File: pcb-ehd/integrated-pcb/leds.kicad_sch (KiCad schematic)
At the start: 41 parts, among them U6 SN74LVC1T45DCK

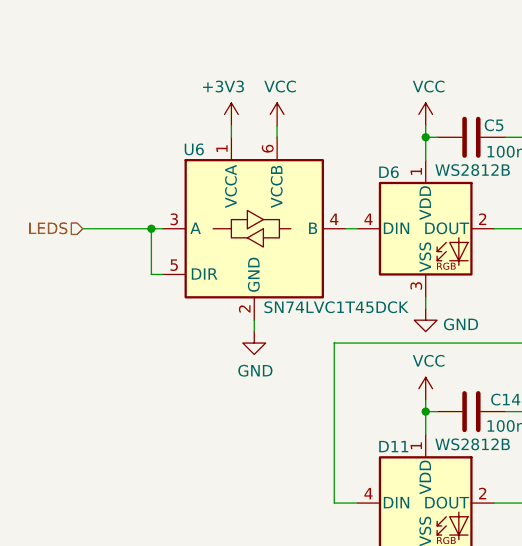
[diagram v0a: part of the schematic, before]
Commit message: rough placement of all but analog
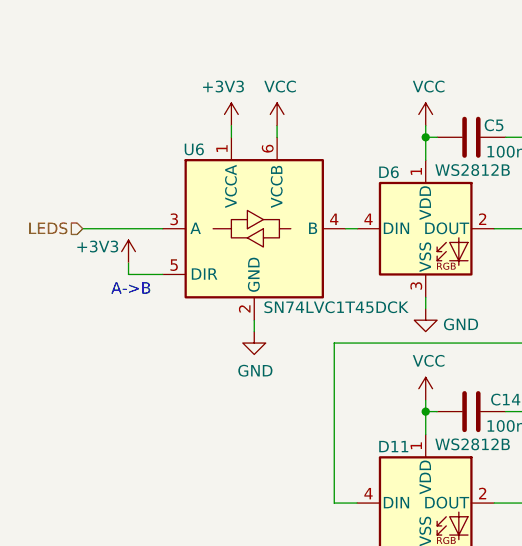
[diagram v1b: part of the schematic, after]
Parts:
- D10, D11, D12, D13, D14, D15, D16, D17, D18, D19, D20, D21, D22, D23, D24, D25, D6, D7, D8, D9: footprint LED_SMD:LED_WS2812B_PLCC4_5.0x5.0mm_P3.2mm -> ehd:LED_WS2812B_PLCC4_5.0x5.0mm_P3.2mm
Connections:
- net +3V3: now also U6.5 (DIR)
- net LEDS: no longer U6.5 (DIR)
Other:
- note added: "A->B"
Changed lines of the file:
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@@
     (company "Josh Johnson")
   )
-  (junction (at 77.47 53.34) (diameter 0.9144) (color 0 0 0 0))
   (junction (at 107.95 43.18) (diameter 0.9144) (color 0 0 0 0))
   (junction (at 107.95 73.66) (diameter 0.9144) (color 0 0 0 0))
@@
   (junction (at 189.23 134.62) (diameter 0.9144) (color 0 0 0 0))
   (no_connect (at 196.85 144.78))
-  (wire (pts (xy 69.85 53.34) (xy 77.47 53.34))
-    (stroke (width 0) (type solid) (color 0 0 0 0))
-  )
-  (wire (pts (xy 77.47 53.34) (xy 77.47 58.42))
-    (stroke (width 0) (type solid) (color 0 0 0 0))
-  )
-  (wire (pts (xy 77.47 53.34) (xy 78.74 53.34))
-    (stroke (width 0) (type solid) (color 0 0 0 0))
-  )
-  (wire (pts (xy 78.74 58.42) (xy 77.47 58.42))
+  (wire (pts (xy 69.85 53.34) (xy 78.74 53.34))
+    (stroke (width 0) (type solid) (color 0 0 0 0))
+  )
+  (wire (pts (xy 74.93 58.42) (xy 74.93 57.15))
+    (stroke (width 0) (type solid) (color 0 0 0 0))
+  )
+  (wire (pts (xy 74.93 58.42) (xy 78.74 58.42))
     (stroke (width 0) (type solid) (color 0 0 0 0))
   )
@@
   (wire (pts (xy 201.93 135.89) (xy 201.93 134.62))
     (stroke (width 0) (type solid) (color 0 0 0 0))
+  )
+  (text "A->B" (at 77.47 60.96 180)
+    (effects (font (size 1.27 1.27)) (justify right bottom))
   )
   (text "Bow Tie LEDs" (at 157.48 34.29 180)
@@
   (hierarchical_label "LEDS" (shape input) (at 69.85 53.34 180)
     (effects (font (size 1.27 1.27)) (justify right))
+  )
+  (symbol (lib_id "power:+3V3") (at 74.93 57.15 0) (unit 1)
+    (in_bom yes) (on_board yes)
+    (property "Reference" "#PWR0197" (id 0) (at 74.93 60.96 0)
+      (effects (font (size 1.27 1.27)) hide)
+    )
+    (property "Value" "+3V3" (id 1) (at 71.4883 55.3656 0))
+    (property "Footprint" "" (id 2) (at 74.93 57.15 0)
+      (effects (font (size 1.27 1.27)) hide)
+    )
+    (property "Datasheet" "" (id 3) (at 74.93 57.15 0)
+      (effects (font (size 1.27 1.27)) hide)
+    )
+    (pin "1")
   )
   (symbol (lib_id "power:+3V3") (at 86.36 41.91 0) (unit 1)
@@
       (effects (font (size 1.27 1.27)) (justify left))
     )
-    (property "Footprint" "LED_SMD:LED_WS2812B_PLCC4_5.0x5.0mm_P3.2mm" (id 2) (at 109.22 60.96 0)
+    (property "Footprint" "ehd:LED_WS2812B_PLCC4_5.0x5.0mm_P3.2mm" (id 2) (at 109.22 60.96 0)
       (effects (font (size 1.27 1.27)) (justify left top) hide)
     )
@@
       (effects (font (size 1.27 1.27)) (justify left))
     )
-    (property "Footprint" "LED_SMD:LED_WS2812B_PLCC4_5.0x5.0mm_P3.2mm" (id 2) (at 109.22 91.44 0)
+    (property "Footprint" "ehd:LED_WS2812B_PLCC4_5.0x5.0mm_P3.2mm" (id 2) (at 109.22 91.44 0)
       (effects (font (size 1.27 1.27)) (justify left top) hide)
     )
@@
       (effects (font (size 1.27 1.27)) (justify left))
     )
-    (property "Footprint" "LED_SMD:LED_WS2812B_PLCC4_5.0x5.0mm_P3.2mm" (id 2) (at 109.22 121.92 0)
+    (property "Footprint" "ehd:LED_WS2812B_PLCC4_5.0x5.0mm_P3.2mm" (id 2) (at 109.22 121.92 0)
       (effects (font (size 1.27 1.27)) (justify left top) hide)
     )
@@
       (effects (font (size 1.27 1.27)) (justify left))
     )
-    (property "Footprint" "LED_SMD:LED_WS2812B_PLCC4_5.0x5.0mm_P3.2mm" (id 2) (at 109.22 152.4 0)
+    (property "Footprint" "ehd:LED_WS2812B_PLCC4_5.0x5.0mm_P3.2mm" (id 2) (at 109.22 152.4 0)
       (effects (font (size 1.27 1.27)) (justify left top) hide)
     )
@@
       (effects (font (size 1.27 1.27)) (justify left))
     )
-    (property "Footprint" "LED_SMD:LED_WS2812B_PLCC4_5.0x5.0mm_P3.2mm" (id 2) (at 129.54 60.96 0)
+    (property "Footprint" "ehd:LED_WS2812B_PLCC4_5.0x5.0mm_P3.2mm" (id 2) (at 129.54 60.96 0)
       (effects (font (size 1.27 1.27)) (justify left top) hide)
     )
@@
       (effects (font (size 1.27 1.27)) (justify left))
     )
-    (property "Footprint" "LED_SMD:LED_WS2812B_PLCC4_5.0x5.0mm_P3.2mm" (id 2) (at 129.54 91.44 0)
+    (property "Footprint" "ehd:LED_WS2812B_PLCC4_5.0x5.0mm_P3.2mm" (id 2) (at 129.54 91.44 0)
       (effects (font (size 1.27 1.27)) (justify left top) hide)
     )
@@
       (effects (font (size 1.27 1.27)) (justify left))
     )
-    (property "Footprint" "LED_SMD:LED_WS2812B_PLCC4_5.0x5.0mm_P3.2mm" (id 2) (at 129.54 121.92 0)
+    (property "Footprint" "ehd:LED_WS2812B_PLCC4_5.0x5.0mm_P3.2mm" (id 2) (at 129.54 121.92 0)
       (effects (font (size 1.27 1.27)) (justify left top) hide)
     )
@@
       (effects (font (size 1.27 1.27)) (justify left))
     )
-    (property "Footprint" "LED_SMD:LED_WS2812B_PLCC4_5.0x5.0mm_P3.2mm" (id 2) (at 129.54 152.4 0)
+    (property "Footprint" "ehd:LED_WS2812B_PLCC4_5.0x5.0mm_P3.2mm" (id 2) (at 129.54 152.4 0)
       (effects (font (size 1.27 1.27)) (justify left top) hide)
     )
@@
       (effects (font (size 1.27 1.27)) (justify left))
     )
-    (property "Footprint" "LED_SMD:LED_WS2812B_PLCC4_5.0x5.0mm_P3.2mm" (id 2) (at 149.86 60.96 0)
+    (property "Footprint" "ehd:LED_WS2812B_PLCC4_5.0x5.0mm_P3.2mm" (id 2) (at 149.86 60.96 0)
       (effects (font (size 1.27 1.27)) (justify left top) hide)
     )
@@
       (effects (font (size 1.27 1.27)) (justify left))
     )
-    (property "Footprint" "LED_SMD:LED_WS2812B_PLCC4_5.0x5.0mm_P3.2mm" (id 2) (at 149.86 91.44 0)
+    (property "Footprint" "ehd:LED_WS2812B_PLCC4_5.0x5.0mm_P3.2mm" (id 2) (at 149.86 91.44 0)
       (effects (font (size 1.27 1.27)) (justify left top) hide)
     )
@@
       (effects (font (size 1.27 1.27)) (justify left))
     )
-    (property "Footprint" "LED_SMD:LED_WS2812B_PLCC4_5.0x5.0mm_P3.2mm" (id 2) (at 149.86 121.92 0)
+    (property "Footprint" "ehd:LED_WS2812B_PLCC4_5.0x5.0mm_P3.2mm" (id 2) (at 149.86 121.92 0)
       (effects (font (size 1.27 1.27)) (justify left top) hide)
     )
@@
       (effects (font (size 1.27 1.27)) (justify left))
     )
-    (property "Footprint" "LED_SMD:LED_WS2812B_PLCC4_5.0x5.0mm_P3.2mm" (id 2) (at 149.86 152.4 0)
+    (property "Footprint" "ehd:LED_WS2812B_PLCC4_5.0x5.0mm_P3.2mm" (id 2) (at 149.86 152.4 0)
       (effects (font (size 1.27 1.27)) (justify left top) hide)
     )
@@
       (effects (font (size 1.27 1.27)) (justify left))
     )
-    (property "Footprint" "LED_SMD:LED_WS2812B_PLCC4_5.0x5.0mm_P3.2mm" (id 2) (at 170.18 60.96 0)
+    (property "Footprint" "ehd:LED_WS2812B_PLCC4_5.0x5.0mm_P3.2mm" (id 2) (at 170.18 60.96 0)
       (effects (font (size 1.27 1.27)) (justify left top) hide)
     )
@@
       (effects (font (size 1.27 1.27)) (justify left))
     )
-    (property "Footprint" "LED_SMD:LED_WS2812B_PLCC4_5.0x5.0mm_P3.2mm" (id 2) (at 170.18 91.44 0)
+    (property "Footprint" "ehd:LED_WS2812B_PLCC4_5.0x5.0mm_P3.2mm" (id 2) (at 170.18 91.44 0)
       (effects (font (size 1.27 1.27)) (justify left top) hide)
     )
@@
       (effects (font (size 1.27 1.27)) (justify left))
     )
-    (property "Footprint" "LED_SMD:LED_WS2812B_PLCC4_5.0x5.0mm_P3.2mm" (id 2) (at 170.18 121.92 0)
+    (property "Footprint" "ehd:LED_WS2812B_PLCC4_5.0x5.0mm_P3.2mm" (id 2) (at 170.18 121.92 0)
       (effects (font (size 1.27 1.27)) (justify left top) hide)
     )
@@
       (effects (font (size 1.27 1.27)) (justify left))
     )
-    (property "Footprint" "LED_SMD:LED_WS2812B_PLCC4_5.0x5.0mm_P3.2mm" (id 2) (at 170.18 152.4 0)
+    (property "Footprint" "ehd:LED_WS2812B_PLCC4_5.0x5.0mm_P3.2mm" (id 2) (at 170.18 152.4 0)
       (effects (font (size 1.27 1.27)) (justify left top) hide)
     )
@@
       (effects (font (size 1.27 1.27)) (justify left))
     )
-    (property "Footprint" "LED_SMD:LED_WS2812B_PLCC4_5.0x5.0mm_P3.2mm" (id 2) (at 190.5 60.96 0)
+    (property "Footprint" "ehd:LED_WS2812B_PLCC4_5.0x5.0mm_P3.2mm" (id 2) (at 190.5 60.96 0)
       (effects (font (size 1.27 1.27)) (justify left top) hide)
     )
@@
       (effects (font (size 1.27 1.27)) (justify left))
     )
-    (property "Footprint" "LED_SMD:LED_WS2812B_PLCC4_5.0x5.0mm_P3.2mm" (id 2) (at 190.5 91.44 0)
+    (property "Footprint" "ehd:LED_WS2812B_PLCC4_5.0x5.0mm_P3.2mm" (id 2) (at 190.5 91.44 0)
       (effects (font (size 1.27 1.27)) (justify left top) hide)
     )
@@
       (effects (font (size 1.27 1.27)) (justify left))
     )
-    (property "Footprint" "LED_SMD:LED_WS2812B_PLCC4_5.0x5.0mm_P3.2mm" (id 2) (at 190.5 121.92 0)
+    (property "Footprint" "ehd:LED_WS2812B_PLCC4_5.0x5.0mm_P3.2mm" (id 2) (at 190.5 121.92 0)
       (effects (font (size 1.27 1.27)) (justify left top) hide)
     )
@@
       (effects (font (size 1.27 1.27)) (justify left))
     )
-    (property "Footprint" "LED_SMD:LED_WS2812B_PLCC4_5.0x5.0mm_P3.2mm" (id 2) (at 190.5 152.4 0)
-      (effects (font (size 1.27 1.27)) (justify left top) hide)
-    )
+    (property "Footprint" "ehd:LED_WS2812B_PLCC4_5.0x5.0mm_P3.2mm" (id 2) (at 190.5 152.4 0)
+      (effects (font (size 1.27 1.27)) (justify left top) hide)
+    )

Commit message: cleanup kicad files
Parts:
- D10, D11, D12, D13, D14, D15, D16, D17, D18, D19, D20, D21, D22, D23, D24, D25, D6, D7, D8, D9: LCSC (none) -> C114586; MPN (none) -> WS2812B-B; Manufacturer (none) -> Worldsemi
- U6: LCSC (none) -> C80768; MPN (none) -> SN74LVC1T45DCKT; Manufacturer (none) -> Texas Instruments
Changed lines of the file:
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@@
       (effects (font (size 1.27 1.27)) (justify left top) hide)
+    )
+    (property "LCSC" "C114586" (id 4) (at 107.95 53.34 0)
+      (effects (font (size 1.27 1.27)) hide)
+    )
+    (property "MPN" "WS2812B-B" (id 5) (at 107.95 53.34 0)
+      (effects (font (size 1.27 1.27)) hide)
+    )
+    (property "Manufacturer" "Worldsemi" (id 6) (at 107.95 53.34 0)
+      (effects (font (size 1.27 1.27)) hide)
     )
     (pin "1")
@@
       (effects (font (size 1.27 1.27)) (justify left top) hide)
     )
+    (property "LCSC" "C114586" (id 4) (at 107.95 83.82 0)
+      (effects (font (size 1.27 1.27)) hide)
+    )
+    (property "MPN" "WS2812B-B" (id 5) (at 107.95 83.82 0)
+      (effects (font (size 1.27 1.27)) hide)
+    )
+    (property "Manufacturer" "Worldsemi" (id 6) (at 107.95 83.82 0)
+      (effects (font (size 1.27 1.27)) hide)
+    )
     (pin "1")
     (pin "2")
@@
       (effects (font (size 1.27 1.27)) (justify left top) hide)
     )
+    (property "LCSC" "C114586" (id 4) (at 107.95 114.3 0)
+      (effects (font (size 1.27 1.27)) hide)
+    )
+    (property "MPN" "WS2812B-B" (id 5) (at 107.95 114.3 0)
+      (effects (font (size 1.27 1.27)) hide)
+    )
+    (property "Manufacturer" "Worldsemi" (id 6) (at 107.95 114.3 0)
+      (effects (font (size 1.27 1.27)) hide)
+    )
     (pin "1")
     (pin "2")
@@
       (effects (font (size 1.27 1.27)) (justify left top) hide)
     )
+    (property "LCSC" "C114586" (id 4) (at 107.95 144.78 0)
+      (effects (font (size 1.27 1.27)) hide)
+    )
+    (property "MPN" "WS2812B-B" (id 5) (at 107.95 144.78 0)
+      (effects (font (size 1.27 1.27)) hide)
+    )
+    (property "Manufacturer" "Worldsemi" (id 6) (at 107.95 144.78 0)
+      (effects (font (size 1.27 1.27)) hide)
+    )
     (pin "1")
     (pin "2")
@@
       (effects (font (size 1.27 1.27)) (justify left top) hide)
     )
+    (property "LCSC" "C114586" (id 4) (at 128.27 53.34 0)
+      (effects (font (size 1.27 1.27)) hide)
+    )
+    (property "MPN" "WS2812B-B" (id 5) (at 128.27 53.34 0)
+      (effects (font (size 1.27 1.27)) hide)
+    )
+    (property "Manufacturer" "Worldsemi" (id 6) (at 128.27 53.34 0)
+      (effects (font (size 1.27 1.27)) hide)
+    )
     (pin "1")
     (pin "2")
@@
       (effects (font (size 1.27 1.27)) (justify left top) hide)
     )
+    (property "LCSC" "C114586" (id 4) (at 128.27 83.82 0)
+      (effects (font (size 1.27 1.27)) hide)
+    )
+    (property "MPN" "WS2812B-B" (id 5) (at 128.27 83.82 0)
+      (effects (font (size 1.27 1.27)) hide)
+    )
+    (property "Manufacturer" "Worldsemi" (id 6) (at 128.27 83.82 0)
+      (effects (font (size 1.27 1.27)) hide)
+    )
     (pin "1")
     (pin "2")
@@
       (effects (font (size 1.27 1.27)) (justify left top) hide)
     )
+    (property "LCSC" "C114586" (id 4) (at 128.27 114.3 0)
+      (effects (font (size 1.27 1.27)) hide)
+    )
+    (property "MPN" "WS2812B-B" (id 5) (at 128.27 114.3 0)
+      (effects (font (size 1.27 1.27)) hide)
+    )
+    (property "Manufacturer" "Worldsemi" (id 6) (at 128.27 114.3 0)
+      (effects (font (size 1.27 1.27)) hide)
+    )
     (pin "1")
     (pin "2")
@@
       (effects (font (size 1.27 1.27)) (justify left top) hide)
     )
+    (property "LCSC" "C114586" (id 4) (at 128.27 144.78 0)
+      (effects (font (size 1.27 1.27)) hide)
+    )
+    (property "MPN" "WS2812B-B" (id 5) (at 128.27 144.78 0)
+      (effects (font (size 1.27 1.27)) hide)
+    )
+    (property "Manufacturer" "Worldsemi" (id 6) (at 128.27 144.78 0)
+      (effects (font (size 1.27 1.27)) hide)
+    )
     (pin "1")
     (pin "2")
@@
       (effects (font (size 1.27 1.27)) (justify left top) hide)
     )
+    (property "LCSC" "C114586" (id 4) (at 148.59 53.34 0)
+      (effects (font (size 1.27 1.27)) hide)
+    )
+    (property "MPN" "WS2812B-B" (id 5) (at 148.59 53.34 0)
+      (effects (font (size 1.27 1.27)) hide)
+    )
+    (property "Manufacturer" "Worldsemi" (id 6) (at 148.59 53.34 0)
+      (effects (font (size 1.27 1.27)) hide)
+    )
     (pin "1")
     (pin "2")
@@
       (effects (font (size 1.27 1.27)) (justify left top) hide)
     )
+    (property "LCSC" "C114586" (id 4) (at 148.59 83.82 0)
+      (effects (font (size 1.27 1.27)) hide)
+    )
+    (property "MPN" "WS2812B-B" (id 5) (at 148.59 83.82 0)
+      (effects (font (size 1.27 1.27)) hide)
+    )
+    (property "Manufacturer" "Worldsemi" (id 6) (at 148.59 83.82 0)
+      (effects (font (size 1.27 1.27)) hide)
+    )
     (pin "1")
     (pin "2")
@@
       (effects (font (size 1.27 1.27)) (justify left top) hide)
     )
+    (property "LCSC" "C114586" (id 4) (at 148.59 114.3 0)
+      (effects (font (size 1.27 1.27)) hide)
+    )
+    (property "MPN" "WS2812B-B" (id 5) (at 148.59 114.3 0)
+      (effects (font (size 1.27 1.27)) hide)
+    )
+    (property "Manufacturer" "Worldsemi" (id 6) (at 148.59 114.3 0)
+      (effects (font (size 1.27 1.27)) hide)
+    )
     (pin "1")
     (pin "2")
@@
       (effects (font (size 1.27 1.27)) (justify left top) hide)
     )
+    (property "LCSC" "C114586" (id 4) (at 148.59 144.78 0)
+      (effects (font (size 1.27 1.27)) hide)
+    )
+    (property "MPN" "WS2812B-B" (id 5) (at 148.59 144.78 0)
+      (effects (font (size 1.27 1.27)) hide)
+    )
+    (property "Manufacturer" "Worldsemi" (id 6) (at 148.59 144.78 0)
+      (effects (font (size 1.27 1.27)) hide)
+    )
     (pin "1")
     (pin "2")
@@
       (effects (font (size 1.27 1.27)) (justify left top) hide)
     )
+    (property "LCSC" "C114586" (id 4) (at 168.91 53.34 0)
+      (effects (font (size 1.27 1.27)) hide)
+    )
+    (property "MPN" "WS2812B-B" (id 5) (at 168.91 53.34 0)
+      (effects (font (size 1.27 1.27)) hide)
+    )
+    (property "Manufacturer" "Worldsemi" (id 6) (at 168.91 53.34 0)
+      (effects (font (size 1.27 1.27)) hide)
+    )
     (pin "1")
     (pin "2")
@@
       (effects (font (size 1.27 1.27)) (justify left top) hide)
     )
+    (property "LCSC" "C114586" (id 4) (at 168.91 83.82 0)
+      (effects (font (size 1.27 1.27)) hide)
+    )
+    (property "MPN" "WS2812B-B" (id 5) (at 168.91 83.82 0)
+      (effects (font (size 1.27 1.27)) hide)
+    )
+    (property "Manufacturer" "Worldsemi" (id 6) (at 168.91 83.82 0)
+      (effects (font (size 1.27 1.27)) hide)
+    )
     (pin "1")
     (pin "2")
@@
       (effects (font (size 1.27 1.27)) (justify left top) hide)
     )
+    (property "LCSC" "C114586" (id 4) (at 168.91 114.3 0)
+      (effects (font (size 1.27 1.27)) hide)
+    )
+    (property "MPN" "WS2812B-B" (id 5) (at 168.91 114.3 0)
+      (effects (font (size 1.27 1.27)) hide)
+    )
+    (property "Manufacturer" "Worldsemi" (id 6) (at 168.91 114.3 0)
+      (effects (font (size 1.27 1.27)) hide)
+    )
     (pin "1")
     (pin "2")
@@
       (effects (font (size 1.27 1.27)) (justify left top) hide)
     )
+    (property "LCSC" "C114586" (id 4) (at 168.91 144.78 0)
+      (effects (font (size 1.27 1.27)) hide)
+    )
+    (property "MPN" "WS2812B-B" (id 5) (at 168.91 144.78 0)
+      (effects (font (size 1.27 1.27)) hide)
+    )
+    (property "Manufacturer" "Worldsemi" (id 6) (at 168.91 144.78 0)
+      (effects (font (size 1.27 1.27)) hide)
+    )
     (pin "1")
     (pin "2")
@@
       (effects (font (size 1.27 1.27)) (justify left top) hide)
     )
+    (property "LCSC" "C114586" (id 4) (at 189.23 53.34 0)
+      (effects (font (size 1.27 1.27)) hide)
+    )
+    (property "MPN" "WS2812B-B" (id 5) (at 189.23 53.34 0)
+      (effects (font (size 1.27 1.27)) hide)
+    )
+    (property "Manufacturer" "Worldsemi" (id 6) (at 189.23 53.34 0)
+      (effects (font (size 1.27 1.27)) hide)
+    )
     (pin "1")
     (pin "2")
@@
       (effects (font (size 1.27 1.27)) (justify left top) hide)
     )
+    (property "LCSC" "C114586" (id 4) (at 189.23 83.82 0)
+      (effects (font (size 1.27 1.27)) hide)
+    )
+    (property "MPN" "WS2812B-B" (id 5) (at 189.23 83.82 0)
+      (effects (font (size 1.27 1.27)) hide)
+    )
+    (property "Manufacturer" "Worldsemi" (id 6) (at 189.23 83.82 0)
+      (effects (font (size 1.27 1.27)) hide)
+    )
     (pin "1")
     (pin "2")
@@
       (effects (font (size 1.27 1.27)) (justify left top) hide)
     )
+    (property "LCSC" "C114586" (id 4) (at 189.23 114.3 0)
+      (effects (font (size 1.27 1.27)) hide)
+    )
+    (property "MPN" "WS2812B-B" (id 5) (at 189.23 114.3 0)
+      (effects (font (size 1.27 1.27)) hide)
+    )
+    (property "Manufacturer" "Worldsemi" (id 6) (at 189.23 114.3 0)
+      (effects (font (size 1.27 1.27)) hide)
+    )
     (pin "1")
     (pin "2")
@@
       (effects (font (size 1.27 1.27)) (justify left top) hide)
     )
+    (property "LCSC" "C114586" (id 4) (at 189.23 144.78 0)
+      (effects (font (size 1.27 1.27)) hide)
+    )
+    (property "MPN" "WS2812B-B" (id 5) (at 189.23 144.78 0)
+      (effects (font (size 1.27 1.27)) hide)
+    )
+    (property "Manufacturer" "Worldsemi" (id 6) (at 189.23 144.78 0)
+      (effects (font (size 1.27 1.27)) hide)
+    )
     (pin "1")
     (pin "2")
@@
       (effects (font (size 1.27 1.27)) hide)
     )
+    (property "LCSC" "C80768" (id 4) (at 88.9 53.34 0)
+      (effects (font (size 1.27 1.27)) hide)
+    )
+    (property "MPN" "SN74LVC1T45DCKT" (id 5) (at 88.9 53.34 0)
+      (effects (font (size 1.27 1.27)) hide)
+    )
+    (property "Manufacturer" "Texas Instruments" (id 6) (at 88.9 53.34 0)
+      (effects (font (size 1.27 1.27)) hide)
+    )
